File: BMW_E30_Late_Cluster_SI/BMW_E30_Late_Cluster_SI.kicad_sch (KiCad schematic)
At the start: 91 parts, among them J1 SI LED Board, J5 Nexus Connector, Q11 BC327-16, Q12 BC337-25, Q13 BC337-16, Q14 BC547B, Q15 BC557B, Q17 BC337-25, Q19 BC337-25, Q21 BC337-25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

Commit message: Started with Schematic Diagram
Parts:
- added BT1, BT2: 3V, symbol Device:Battery_Cell
- added D24: SD103A, symbol Device:D
- added D3: BAV21, Diode_THT:D_DO-35_SOD27_P7.62mm_Horizontal, symbol Diode:BAV21
- added J2: Coding Plug, symbol Connector_Generic:Conn_01x08
- added R21: 10k, SI_THT:R_Axial_Narrow_L6.8mm_D2.4mm_P9.7mm, symbol Device:R
- U1: footprint Package_TO_SOT_THT:TO-92_Inline -> Package_TO_SOT_THT:TO-92_Inline_Wide
- renumbered D3 to D8
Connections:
- net +12_T15: now also D4.2 (A)
- net +12_T30: now also D2.2 (A)
- net GNDPWR: now also C2.2, U1.2 (GND)
- net at D4.1 (K): now also R3.1, D3.2 (A)
- net at R4.1: now also Q11.2 (B)
- net at R4.2: now also Q11.3 (E), R21.1
- net at D2.1 (K): now also R1.2, D3.1 (K)
- net +5V: now reaches Q19.2 (B)
- net +5V: now also U1.1 (VO)
- net at Q11.1 (C): now also R6.2
- net VCC_T15: now reaches R3.2
- net VCC_T30: now reaches R1.1
- net VCC_T30: now also C2.1, U1.3 (VI)
- net at Q14.2 (B): now also R22.2, R21.2
- net at Q14.3 (E): now also R22.1
- new net: BT1.2 (-), BT2.1 (+)
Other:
- moved on the sheet: C1, C10, C11, C12, C13, C14, C15, C17, C18, C19, C2, C20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

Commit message: Update SI Schematic
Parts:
- added D26: LED, symbol Device:LED
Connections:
- net +12_T30: now also D1.2 (A)
- net +5V: now also C15.1, J2.6 (Pin_6)
- net GNDPWR: now also C10.2, C11.2, C13.2, C15.2, C17.2, Q14.3 (E), R22.1
- net VCC_T15: now also D18.2 (A), J1.1 (Pin_1), R29.1
- net at D1.1 (K): now also R27.1
- net at C11.1: now also R24.2, R25.1
- net at R26.1: now also Q15.3 (E)
- net at R26.2: now also R23.1
- net IC3_P7: now reaches C13.1
- net IC3_P7: now also C10.1, C17.1, Q17.3 (E), R20.1
- net SI_LED_P2: now reaches J1.2 (Pin_2)
- net SI_LED_P2: now also Q19.3 (E)
- net IC1_P18: now reaches Q17.1 (C)
- net at Q17.2 (B): now also Q15.1 (C)
- net IC4_P25: now reaches R27.2
- net IC4_P25: now also D26.2 (A)
- net at R23.2: now also Q15.2 (B), R24.1
- net IC1_P23: now reaches R20.2
- net at Q19.1 (C): now also R30.2
- net at C21.1: now also R46.1, D26.1 (K)
- net IC4_P21: now reaches C21.2
- net IC4_P21: now also R46.2
- net at C14.1: now also R29.2
- net at R30.1: now also D18.1 (K)
- net at Q14.1 (C): now also R25.2
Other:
- moved on the sheet: BT1, BT2, C10, C11, C13, C14, C15, C17, C21, D1, D18, J1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

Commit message: Updates to SI Schematic Layout
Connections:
- net GNDPWR: now also C14.2, C4.2, C8.2, D16.2 (A), D8.2 (A), Q12.3 (E), Q22.3 (E), Q23.3 (E), R13.2, R18.2, R28.2
- net IC1_P18: now also R10.2, R9.1
- net VCC_T15: now also C4.1, Q11.3 (E), R10.1, R21.1, R4.2
- net at D1.1 (K), R27.1: now also R23.1, R26.2
- net at Q11.2 (B), R4.1: now also R5.1
- net at Q15.1 (C), Q17.2 (B): now also D16.1 (K), R28.1
- net at Q12.1 (C): now also R5.2
- net at Q12.2 (B): now also R9.2
- net IC4_P36: now reaches C14.1, R29.2
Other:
- moved on the sheet: BT1, BT2, C10, C11, C13, C14, C17, C21, C4, C8, D1, D16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

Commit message: Updates to SI Schematic
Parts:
- added JP1: Battery Jumper, symbol Jumper:Jumper_3_Bridged12
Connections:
- net +5V: now also JP1.1 (A)
- net Eng_temp_sensor: now also D8.1 (K), R16.1, R17.1, R18.1
- net GNDPWR: now also Q13.3 (E), Q21.3 (E)
- net IC1_P18: now also Q13.2 (B)
- net IC4_P21: now also R34.1
- net IC4_P25: now also BT1.2 (-), BT2.2 (-), C18.2
- net Temp_GND: now also Q13.1 (C)
- net IC1_P17: now reaches R16.2
- net at R34.2: now also J1.7 (Pin_7)
- net at J1.10 (Pin_10): now also Q23.1 (C)
- net at J1.11 (Pin_11): now also Q21.1 (C)
- net at J1.12 (Pin_12): now also R32.2
- net at J1.3 (Pin_3): now also R38.2
- net at J1.4 (Pin_4): now also R37.2
- net at J1.5 (Pin_5): now also R36.2
- net at J1.6 (Pin_6): now also R35.2
- net at J1.8 (Pin_8): now also R33.2
- net at J1.9 (Pin_9): now also Q22.1 (C)
- net IC4_P24: now reaches R38.1
- net at D25.1 (K): now also C18.1, C19.1, C20.1, D24.1 (K), JP1.2 (C)
- net at D25.2 (A): now also BT2.1 (+), C20.2
- net IC4_P18: now reaches R37.1
- net IC4_P14: now reaches R39.1
- net at R39.2: now also Q21.2 (B)
- net at C19.2: now also BT1.1 (+), D24.2 (A)
- net IC1_P19: now reaches C8.1
- net IC1_P19: now also R17.2
- net at Q23.2 (B): now also R41.2
- net IC4_P13: now reaches R40.1
- net at R40.2: now also Q22.2 (B)
- net IC4_P22: now reaches R33.1
- net IC4_P16: now reaches R41.1
- net IC4_P19: now reaches R36.1
- net IC4-P24: now reaches R32.1
- net IC4_P20: now reaches R35.1
- net SI_LED_P2: no longer names the net of J1.2 (Pin_2), Q19.3 (E)
- no-connect marks 1 -> 2
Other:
- moved on the sheet: BT1, BT2, C14, C18, C19, C20, C8, D18, D24, D25, D8, J1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

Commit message: Schematic Progress
All components other than IC's are accounted for in the schematic. There are still IC1 - IC4 that need custom symbols and will have a few more traces in between pins than are currently shown in the schematic. Otherwise the schematic is functionally complete. Working on formatting for readability.
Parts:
- removed C14: 10n, Capacitor_THT:C_Disc_D6.0mm_W2.5mm_P5.00mm, symbol Device:C
- removed D18: 1N4148, symbol Device:D
- removed J1: SI LED Board, Connector_PinHeader_2.54mm:PinHeader_1x12_P2.54mm_Vertical, symbol Connector:Conn_01x12_Pin
- removed Q19, Q21, Q22, Q23: BC337-25, Package_TO_SOT_THT:TO-92_Inline_Wide, symbol Transistor_BJT:BC337
- removed R29: 100k, SI_THT:R_Axial_Narrow_L6.8mm_D2.4mm_P9.7mm, symbol Device:R
- removed R30: 75R, SI_THT:R_Axial_Narrow_L6.8mm_D2.4mm_P9.7mm, symbol Device:R
- removed R32, R33, R34, R35, R36, R37, R38: 160R, SI_THT:R_Axial_Narrow_L6.8mm_D2.4mm_P9.7mm, symbol Device:R
- removed R39, R40, R41: 4k7, SI_THT:R_Axial_Narrow_L6.8mm_D2.4mm_P9.7mm, symbol Device:R
- removed Y2: Crystal, Crystal:Crystal_C38-LF_D3.0mm_L8.0mm_Horizontal, symbol Device:Crystal
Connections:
- net +12_T15: now also C3.1
- net +12_T30: now also C1.1
- net EG_1+: now also R43.1
- net EG_2+: now also R42.1
- net Engine_spd_input: now also R11.1
- net Fuel_rate_input: now also D6.2 (A)
- net GNDPWR: now also C12.2, C5.2, C7.2, D10.2 (A), D7.2 (A), J2.1 (Pin_1), J2.3 (Pin_3), J2.5 (Pin_5), J2.7 (Pin_7), R14.2, R8.2
- net IC1_P17: now also R44.2
- net IC4_P25: now also C12.1
- net SI_RST: now also R19.1
- net Wheel_spd_output: now also D9.1 (K)
- net T30_Protected: now reaches D1.1 (K), R23.1, R26.2, R27.1
- net IC4_P40: now reaches D10.1 (K)
- net IC4_P40: now also C9.2, R19.2
- net at R12.1: now also C6.1, R11.2, R13.1
- net IC1_P22: now reaches R12.2
- net IC1_P22: now also C7.1, D5.1 (K)
- net IGN_Check: now reaches D3.2 (A), D4.1 (K), R3.1
- net IGN_Check: now also R2.1
- net IC1_P4: now reaches J2.2 (Pin_2)
- net IC1_P3: now reaches J2.4 (Pin_4)
- net IC1_P2: now reaches J2.8 (Pin_8)
- net IC2_P12: now reaches R44.1
- net IC2_P12: now also R45.1, Y1.1
- net at C3.2: now also C1.2, C6.2, C9.1, D5.2 (A)
- net IC1_P40: now reaches D7.1 (K)
- net IC1_P40: now also R15.2
- net at R14.1: now also D6.1 (K), R15.1
- net IC1_P20: now reaches R7.1
- net IC1_P20: now also C5.1
- net at R7.2: now also R2.2, R8.1
- net IC3_P24: now reaches R43.2
- net IC3_P21: now reaches R42.2
- net IC1_P39: now reaches D9.2 (A)
- net IC2_P11: now reaches Y1.2
- net IC2_P11: now also R45.2
- net Tach_1+ renamed IC2_P18
- net Tach_1- renamed IC2_P17
- net Tach_2+ renamed IC2_P15
- net Tach_2- renamed IC2_P14
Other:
- added sheet Indicator Lights (Indicator_Lights.kicad_sch)
- moved on the sheet: BT1, BT2, C1, C10, C11, C12, C13, C15, C17, C18, C19, C20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

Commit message: IC's Added to Schematic
IC's added, started going through IC2 (U2), pinouts not complete for these yet as many pins go between chips with no other components involved.
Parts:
- removed BT1, BT2: 3V, symbol Device:Battery_Cell
- removed C12: 100u, Capacitor_THT:CP_Axial_L18.0mm_D6.5mm_P25.00mm_Horizontal, symbol Device:C_Polarized
- removed C18: 0.1u, Capacitor_THT:C_Rect_L7.0mm_W2.0mm_P5.00mm, symbol Device:C
- removed C19, C20, C21: 0.1n, Capacitor_THT:C_Disc_D6.0mm_W2.5mm_P5.00mm, symbol Device:C
- removed D24, D25: SD103A, symbol Device:D
- removed D26: LED, symbol Device:LED
- removed JP1: Battery Jumper, symbol Jumper:Jumper_3_Bridged12
- removed R27: 47R, Resistor_THT:R_Axial_DIN0516_L15.5mm_D5.0mm_P20.32mm_Horizontal, symbol Device:R
- removed R46: 100R, SI_THT:R_Axial_Narrow_L6.8mm_D2.4mm_P9.7mm, symbol Device:R
- added U1: ITT SAF1190-196 MCU, Package_DIP:DIP-40_W15.24mm_LongPads, symbol BMW_ICs:ITT_SAF1190-196_MCU
- added U2: ITT V3003-393, Package_DIP:DIP-16_W10.16mm_LongPads, symbol BMW_ICs:ITT_V3003-393
- added U3: ITT V3004-520, Package_DIP:DIP-24_W15.24mm_LongPads, symbol BMW_ICs:ITT_V3004-520
- renumbered U1 to U5
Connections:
- net +5V: now also J2.3 (Pin_3), U1.1; no longer J2.6 (Pin_6)
- net EG_1-: now also U3.23
- net EG_2-: now also U3.20
- net GNDPWR: now also J2.2 (Pin_2), J2.4 (Pin_4), J2.6 (Pin_6), J2.8 (Pin_8); no longer J2.1 (Pin_1), J2.3 (Pin_3), J2.5 (Pin_5), J2.7 (Pin_7)
- net IC1_P17: now also U1.17; no longer R44.2
- net IC1_P18: now also R10.1, U1.18; no longer Q13.2 (B), R10.2
- net IC1_P19: now also U1.19
- net IC1_P2: now also J2.1 (Pin_1), U1.2; no longer J2.8 (Pin_8)
- net IC1_P20: now also U1.20
- net IC1_P22: now also U1.22
- net IC1_P23: now also U1.23
- net IC1_P3: now also J2.5 (Pin_5), U1.3; no longer J2.4 (Pin_4)
- net IC1_P4: now also J2.7 (Pin_7), U1.4; no longer J2.2 (Pin_2)
- net IC1_P40: now also U1.40
- net IC2_P11: now also U2.11
- net IC2_P12: now also U2.12
- net IC3_P7: now also U2.1, U3.1, U3.7
- net VCC_T15: no longer R10.1
- net IC1_P39: no longer names the net of D9.2 (A)
- net IC1_P39: now also U1.39
- net IC2_P14 renamed Tach_2-
- net Tach_2-: now also U2.14
- net IC2_P15 renamed Tach_2+
- net Tach_2+: now also U2.15
- net IC2_P17 renamed Tach_1-
- net Tach_1-: now also U2.17
- net IC2_P18 renamed Tach_1+
- net Tach_1+: now also U2.18
- net IC3_P21: no longer names the net of R42.2
- net IC3_P21: now also U3.21
- net IC3_P24: no longer names the net of R43.2
- net IC3_P24: now also U3.24
- new net: Q13.2 (B), R10.2
- new net IC1_P31: U1.31, U3.8
- new net IC1_P32: U1.32, U3.9
- new net IC1_P36: U1.36, U3.4
- new net IC1_P37: U1.37, U3.6
- new net IC1_P38: U1.38, U3.5
- new net IC3_P16: R44.2, U2.16
- no-connect marks 2 -> 3
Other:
- sheet Indicator Lights ports: added IC4_P40; removed none
- moved on the sheet: C8, D8, D9, J2, R10, R16, R17, R18, R42, R43, R44, R45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

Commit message: Schematic Functionally Complete
Only changes that should need to be made are formatting and style changes to improve readability.
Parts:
- removed C10, C17: 68n, Capacitor_THT:C_Disc_D6.0mm_W2.5mm_P5.00mm, symbol Device:C
- removed C11: 10u, Capacitor_THT:CP_Radial_Tantal_D9.0mm_P2.50mm, symbol Device:C_Polarized
- removed C13: 47u, Capacitor_THT:CP_Radial_Tantal_D9.0mm_P2.50mm, symbol Device:C_Polarized
- removed C8: 47n, Capacitor_THT:C_Disc_D6.0mm_W2.5mm_P5.00mm, symbol Device:C
- removed D1: 1N4004, Diode_THT:D_DO-41_SOD81_P10.16mm_Horizontal, symbol Diode:1N4004
- removed D16: BZX55C-9V1, symbol Device:D_Zener
- removed D8: ZW 4.7, symbol Device:D_Zener
- removed Q11: BC327-16, Package_TO_SOT_THT:TO-92_Inline_Wide, symbol Transistor_BJT:BC327
- removed Q12, Q17: BC337-25, Package_TO_SOT_THT:TO-92_Inline_Wide, symbol Transistor_BJT:BC337
- removed Q13: BC337-16, Package_TO_SOT_THT:TO-92_Inline_Wide, symbol Transistor_BJT:BC337
- removed Q14: BC547B, Package_TO_SOT_THT:TO-92_Inline_Wide, symbol Transistor_BJT:BC547
- removed Q15: BC557B, Package_TO_SOT_THT:TO-92_Inline_Wide, symbol Transistor_BJT:BC557
- removed R10: 2k2, SI_THT:R_Axial_Narrow_L6.8mm_D2.4mm_P9.7mm, symbol Device:R
- removed R16, R18: 1k5, SI_THT:R_Axial_Narrow_L6.8mm_D2.4mm_P9.7mm, symbol Device:R
- removed R17: 27k, SI_THT:R_Axial_Narrow_L6.8mm_D2.4mm_P9.7mm, symbol Device:R
- removed R20: 22k, Resistor_THT:R_Axial_DIN0207_L6.3mm_D2.5mm_P15.24mm_Horizontal, symbol Device:R
- removed R21: 10k, SI_THT:R_Axial_Narrow_L6.8mm_D2.4mm_P9.7mm, symbol Device:R
- removed R22: 16k, SI_THT:R_Axial_Narrow_L6.8mm_D2.4mm_P9.7mm, symbol Device:R
- removed R23: 39k, SI_THT:R_Axial_Narrow_L6.8mm_D2.4mm_P9.7mm, symbol Device:R
- removed R24: 51k, SI_THT:R_Axial_Narrow_L6.8mm_D2.4mm_P9.7mm, symbol Device:R
- removed R25: 100R, SI_THT:R_Axial_Narrow_L6.8mm_D2.4mm_P9.7mm, symbol Device:R
- removed R26: 1k, SI_THT:R_Axial_Narrow_L6.8mm_D2.4mm_P9.7mm, symbol Device:R
- removed R28: 200R, SI_THT:R_Axial_Narrow_L6.8mm_D2.4mm_P9.7mm, symbol Device:R
- removed R4: 6k8, SI_THT:R_Axial_Narrow_L6.8mm_D2.4mm_P9.7mm, symbol Device:R
- removed R5, R9: 4k6, SI_THT:R_Axial_Narrow_L6.8mm_D2.4mm_P9.7mm, symbol Device:R
- removed R6: 68R, Resistor_THT:R_Axial_DIN0414_L11.9mm_D4.5mm_P20.32mm_Horizontal, symbol Device:R
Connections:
- net GNDPWR: now also U1.21, U2.16, U2.2
- net IC1_P23: now also U2.13
- net IC1_P30: now reaches U2.3
- net IC1_P30: now also U1.30
- net IC1_P29: now reaches U2.4
- net IC1_P29: now also U1.29
- net IC1_P24: now reaches U2.5
- net IC1_P24: now also U1.24
- net IC1_P25: now reaches U2.6
- net IC1_P25: now also U1.25
- net IC1_P26: now reaches U2.7
- net IC1_P26: now also U1.26
- net IC1_P27: now reaches U2.8
- net IC1_P27: now also U1.27
- net IC1_P28: now reaches U2.9
- net IC1_P28: now also U1.28
- net IC4_P30: now reaches U1.11
- net IC4_P38: now reaches U1.12
- net IC4_P37: now reaches U1.13
- net IC4_P35: now reaches U1.14
- net IC4_P34: now reaches U1.15
- net IC4_P15: now reaches U1.16
- net IC1_P33: now reaches U1.33
- net IC1_P33: now also U3.10
- net IC1_P34: now reaches U1.34
- net IC1_P34: now also U3.11
- net IC1_P35: now reaches U1.35
- net IC1_P35: now also U3.13
- net IC4_P32: now reaches U1.5
- net IC4_P29: now reaches U1.6
- net IC4_P39: now reaches U1.8
- net IC4_P12: now reaches U1.9
- net IC3_P17: now reaches U3.17
- net IC3_P17: now also R44.2
- removed net IC3_P16: R44.2, U2.16
- no-connect marks 3 -> 12
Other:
- added sheet Temperature Sensor (Temperature_Sensor.kicad_sch)
- sheet Indicator Lights ports: added IC4_P12, IC4_P15, IC4_P29, IC4_P30, IC4_P32, IC4_P34, IC4_P35, IC4_P37, IC4_P38, IC4_P39; removed none
- moved on the sheet: C1, C3, C5, C6, C7, C9, D10, D5, D6, D7, D9, J2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

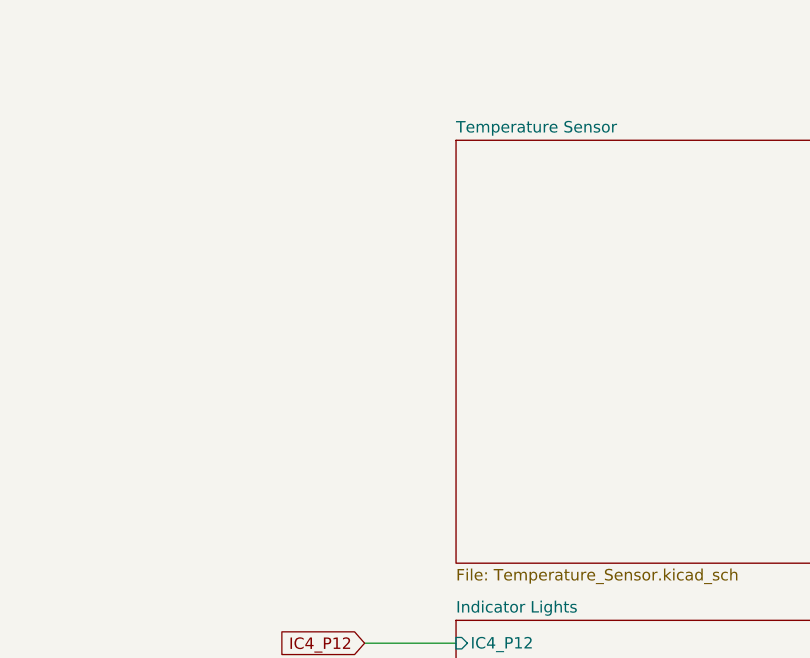
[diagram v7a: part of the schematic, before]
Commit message: Improved Schematic Readability for SI Board
Added final trace flags for readability of the main page. Also exported a BOM for the SI board
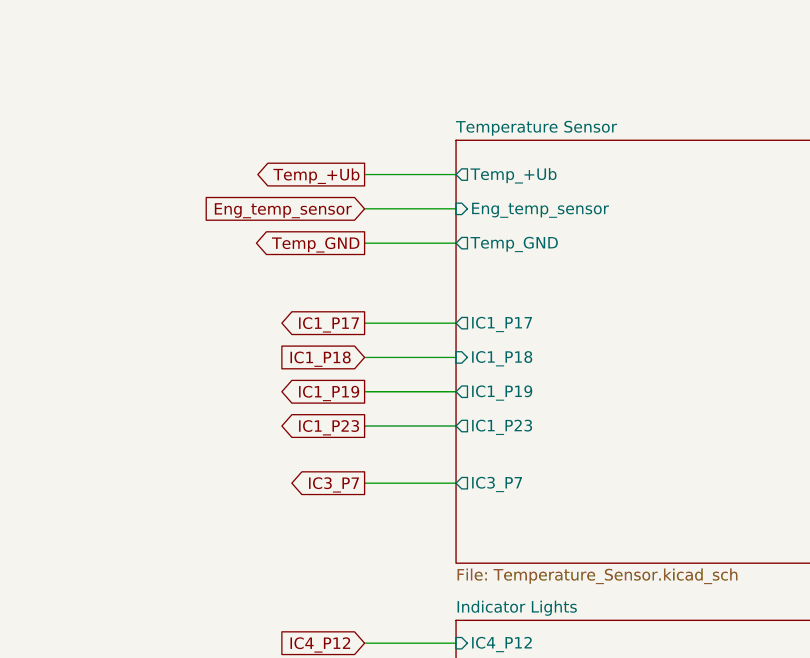
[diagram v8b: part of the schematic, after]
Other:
- sheet Temperature Sensor ports: added Eng_temp_sensor, IC1_P17, IC1_P18, IC1_P19, IC1_P23, IC3_P7, Temp_+Ub, Temp_GND; removed none
